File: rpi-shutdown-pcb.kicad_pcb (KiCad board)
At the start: 2 copper layers, 63.7 x 30 mm, 25 parts, among them IC1 ATTINY85-P, IC2 STEP_DOWN_CONVERTER_(MP2307), P1 CONN_01X03, P2 CONN_01X02, Q1 MOSFET_N_(2N7002P,215), U1 LM3480-3.3

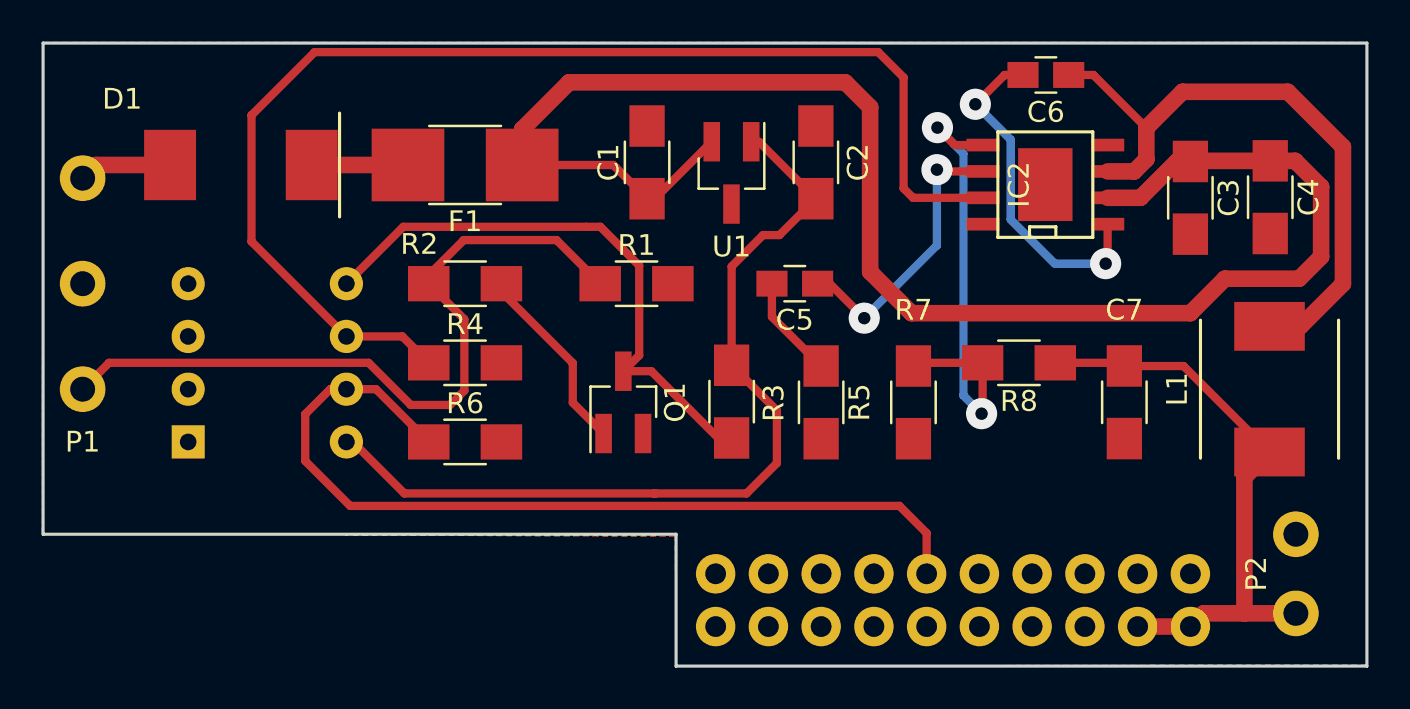
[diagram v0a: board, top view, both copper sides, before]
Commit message: - Rearranged board to hopefully get better voltage regulation.
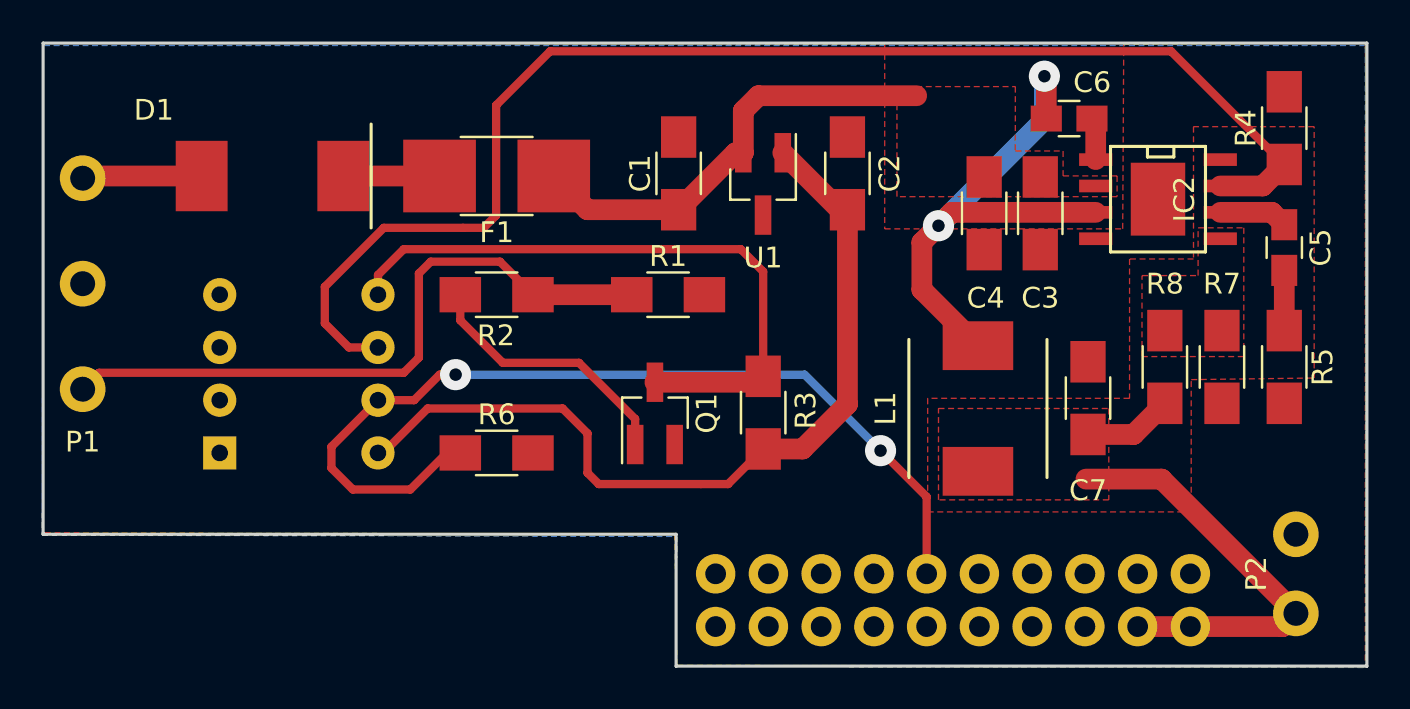
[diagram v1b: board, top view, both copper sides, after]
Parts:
- moved R4 41.0 mm to (193.8, 103.0), turned to 90 degrees
- moved C5 23.6 mm to (193.8, 108.8), turned to 270 degrees
- moved R5 22.4 mm to (193.8, 114.5)
- moved R7 15.0 mm to (190.8, 114.5)
- moved L1 14.1 mm to (179.0, 116.5)
- moved C4 13.8 mm to (179.3, 107.1)
- moved C3 7.27 mm to (182.0, 107.1)
- moved R8 7.03 mm to (188.0, 114.5), turned to 90 degrees
- moved IC2 5.47 mm to (187.7, 106.4), turned to 270 degrees
- moved C6 2.38 mm to (183.4, 102.5), turned to 0 degrees
- moved C7 1.76 mm to (184.3, 116.0), turned to 90 degrees
- moved C2 1.61 mm to (172.7, 105.2)
- moved D1 1.61 mm to (145.0, 105.3)
- moved IC1 1.61 mm to (142.5, 118.6)
- moved R1 1.61 mm to (164.1, 111.0)
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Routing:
- net Net-(C1-Pad1): track 77.3 -> 21.6 mm
- net Net-(IC2-Pad5): track 23.1 -> 0.00 mm, vias 2 -> 0
- net Net-(C6-Pad2): track 16.5 -> 2.05 mm, vias 2 -> 0
- net Net-(C5-Pad1): track 13.8 -> 3.33 mm, vias 2 -> 0
- net Net-(C6-Pad1): track 32.1 -> 26.5 mm, vias 0 -> 2
- net Net-(IC1-Pad6): track 59.6 -> 64.6 mm
- net Net-(Q1-Pad1): track 9.25 -> 12.9 mm
- net Net-(P1-Pad3): track 36.1 -> 33.1 mm
- net Net-(IC1-Pad5): track 28.0 -> 30.8 mm
- net Net-(C7-Pad1): track 28.2 -> 25.9 mm
- net Net-(C5-Pad2): track 4.95 -> 2.90 mm
- net Net-(CONN_1-Pad11): track 43.1 -> 44.6 mm, vias 0 -> 2
- net GND: track 1.33 -> 0.00 mm
- net Net-(D1-Pad2): track 4.47 -> 5.77 mm
- net Net-(C2-Pad1): track 42.5 -> 41.3 mm
- added copper zone on F.Cu, net Net-(C1-Pad1)
- added copper zone on F.Cu, net Net-(C7-Pad1)
- added copper zone on F.Cu, net Net-(IC2-Pad5)
